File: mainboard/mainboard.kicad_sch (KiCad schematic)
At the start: 55 parts, among them J1 Barrel_Jack, J2 USB_C_Receptacle_USB2.0_14P, J3 Conn_01x02, M1 Motor_DC, M2 Motor_DC, M3 Motor_DC, M4 Motor_DC, Q1 2N7002, Q2 2N7002, Q3 2N7002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

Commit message: Prepared for PCB layout
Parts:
- J1: footprint (none) -> Connector_BarrelJack:BarrelJack_GCT_DCJ200-10-A_Horizontal; DPN (none) -> CP-002A-ND; MPN (none) -> PJ-002A
- J2: footprint (none) -> Connector_USB:USB_C_Receptacle_GCT_USB4105-xx-A_16P_TopMnt_Horizontal; DPN (none) -> 2073-USB4105-GF-ACT-ND; MPN (none) -> USB4105-GF-A
- J3: value Conn_01x02 -> Conn_01x04; footprint (none) -> Connector_JST:JST_EH_B4B-EH-A_1x04_P2.50mm_Vertical; DPN (none) -> 455-B4B-XH-A-ND; MPN (none) -> B4B-XH-A
- L1: footprint (none) -> LED_THT:LED_D1.8mm_W1.8mm_H2.4mm_Horizontal_O1.27mm_Z1.6mm
- M1, M2, M3, M4: DPN (none) -> 455-1704-ND; MPN (none) -> B2B-PH-K-S
- R1, R10, R12, R14, R6: DPN (none) -> RMCF0603FT10K0CT-ND; MPN (none) -> RMCF0603FT10K0
- R11: DPN (none) -> RMCF0603FT470RCT-ND; MPN (none) -> RMCF0603FT470R
- R13, R2: DPN (none) -> RMCF0603FT1K00CT-ND; MPN (none) -> RMCF0603FT1K00
- R3: DPN (none) -> 738-RMCF0603FT732KCT-ND; MPN (none) -> RMCF0603FT732K
- R4: DPN (none) -> RMCF0603FT100KCT-ND; MPN (none) -> RMCF0603FT100K
- R5: DPN (none) -> RMCF0603FT33K0CT-ND; MPN (none) -> RMCF0603FT33K0
- R7, R8: DPN (none) -> RMCF0603FT5K10CT-ND; MPN (none) -> RMCF0603FT5K10
- R9: DPN (none) -> RMCF0603FT62K0CT-ND; MPN (none) -> RMCF0603FT62K0
- SW1: footprint (none) -> lib:SW_SPDT; DPN (none) -> 2449-MS1206L6-ND; MPN (none) -> MS1206L6
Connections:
- net GND: now also SW1.3 (C), SW1.M; no longer SW1.1 (A)
- net VBAT: now also SW1.1 (A); no longer SW1.3 (C)

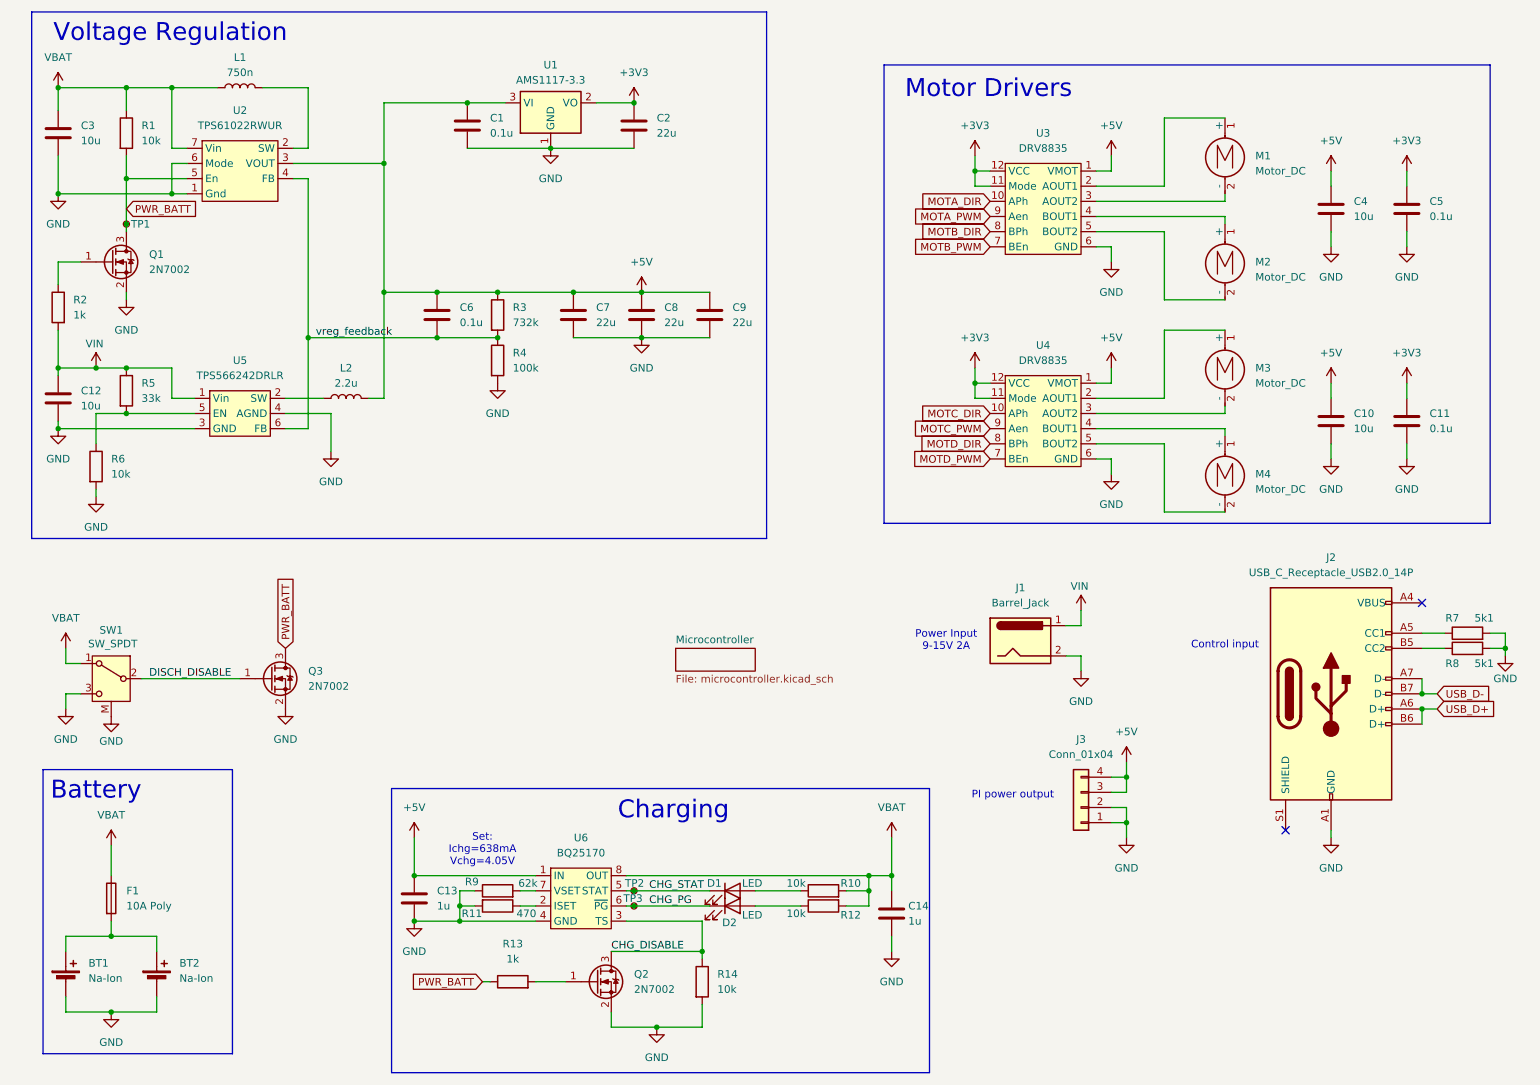
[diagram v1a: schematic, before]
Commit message: Added some 3d libs and started routing
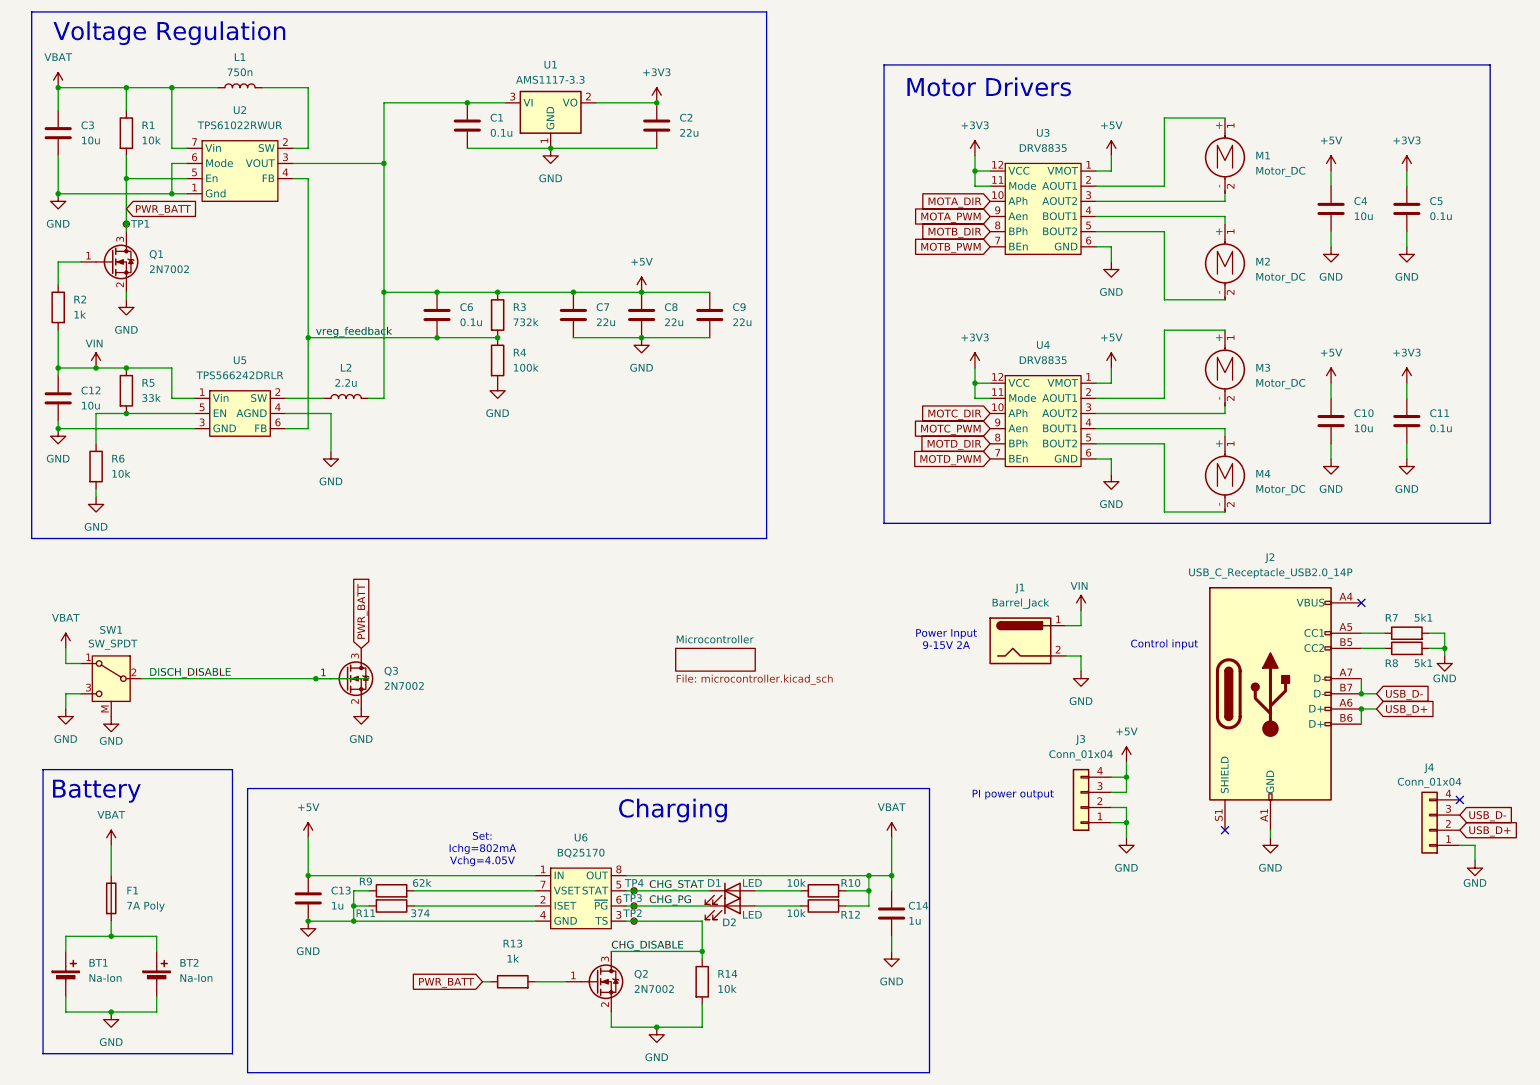
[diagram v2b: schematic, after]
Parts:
- added J4: Conn_01x04, Connector_JST:JST_EH_B4B-EH-A_1x04_P2.50mm_Vertical, symbol Connector_Generic:Conn_01x04
- added TP2: TestPoint_Small, TestPoint:TestPoint_THTPad_1.0x1.0mm_Drill0.5mm, symbol Connector:TestPoint_Small
- F1: value 10A Poly -> 7A Poly; DPN 13-SMD2920B500TF/16CT-ND -> F8138CT-ND; MPN SMD2920B500TF/16 -> 2920L700/12MR
- L1: footprint LED_THT:LED_D1.8mm_W1.8mm_H2.4mm_Horizontal_O1.27mm_Z1.6mm -> lib:inductor_PA431
- L2: footprint Capacitor_SMD:C_0603_1608Metric -> lib:inductor_BMRx
- R11: value 470 -> 374; DPN RMCF0603FT470RCT-ND -> RMCF0603FT374RCT-ND; MPN RMCF0603FT470R -> RMCF0603FT374R
- TP1, TP3: footprint TestPoint:TestPoint_THTPad_2.0x2.0mm_Drill1.0mm -> TestPoint:TestPoint_THTPad_1.0x1.0mm_Drill0.5mm
- TP4: renamed from TP2; footprint TestPoint:TestPoint_THTPad_2.0x2.0mm_Drill1.0mm -> TestPoint:TestPoint_THTPad_1.0x1.0mm_Drill0.5mm
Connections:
- net CHG_DISABLE: now also TP2.1
- net GND: now also J4.1 (Pin_1)
- net USB_D+: now also J4.2 (Pin_2)
- net USB_D-: now also J4.3 (Pin_3)
- no-connect marks 2 -> 3
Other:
- note added: "Set: Ichg=802mA Vchg=4.05V"
- note removed: "Set: Ichg=638mA Vchg=4.05V"
- moved on the sheet: C13, C2, J2, Q3, R11, R7, R8, R9

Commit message: Finished routing
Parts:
- added JP1, JP2: Jumper_2_Bridged, Jumper:SolderJumper-2_P1.3mm_Bridged_Pad1.0x1.5mm, symbol Jumper:Jumper_2_Bridged
- J2: footprint Connector_USB:USB_C_Receptacle_GCT_USB4105-xx-A_16P_TopMnt_Horizontal -> lib:USB_C_Receptacle_USB2
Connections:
- net +3V3: now also JP1.1 (A), JP2.1 (A); no longer U3.11 (Mode), U4.11 (Mode)
- net VUSB: now reaches J2.A4 (VBUS), J2.A9 (VBUS), J2.B4 (VBUS), J2.B9 (VBUS)
- new net: JP2.2 (B), U4.11 (Mode)
- new net: JP1.2 (B), U3.11 (Mode)
- no-connect marks 3 -> 2
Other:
- moved on the sheet: D1, D2, Q2, R13, R14
